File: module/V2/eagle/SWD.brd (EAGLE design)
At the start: 269.1 x 284.5 mm, 273 parts, among them J2 KLDX-0202-A, SW1 MF-SW-TACT-6MM, SW2 MF-SW-TACT-6MM, U1 P8X32A-Q44, U10 SN74LV4066APWR, U11 SN74LV4066APWR, U12 SN74LV4066APWR, U13 SN74LV4066APWR, U14 SN74LV4066APWR, U15 SN74LV4066APWR, U16 SN74LV4066APWR, U17 SN74LV4066APWR, U18 SN74LV4066APWR, U19 SN74LV4066APWR, U2 CAT24C512WI-GT3, U20 SN74LV4066APWR, U21 SN74LV4066APWR, U22 SN74LV4066APWR, U23 SN74LV4066APWR, U24 SSM6J507NU,LF, U25 SSM6J507NU,LF, U26 SSM6J507NU,LF, U27 SSM6J507NU,LF, U3 FT230XQ-R, U4 SN74LV4066APWR, U5 SN74LV4066APWR, U6 SN74LV4066APWR, U7 SN74LV4066APWR, U8 SN74LV4066APWR, U9 SN74LV4066APWR, X1 ABMM-6.000MHZ-B2-T

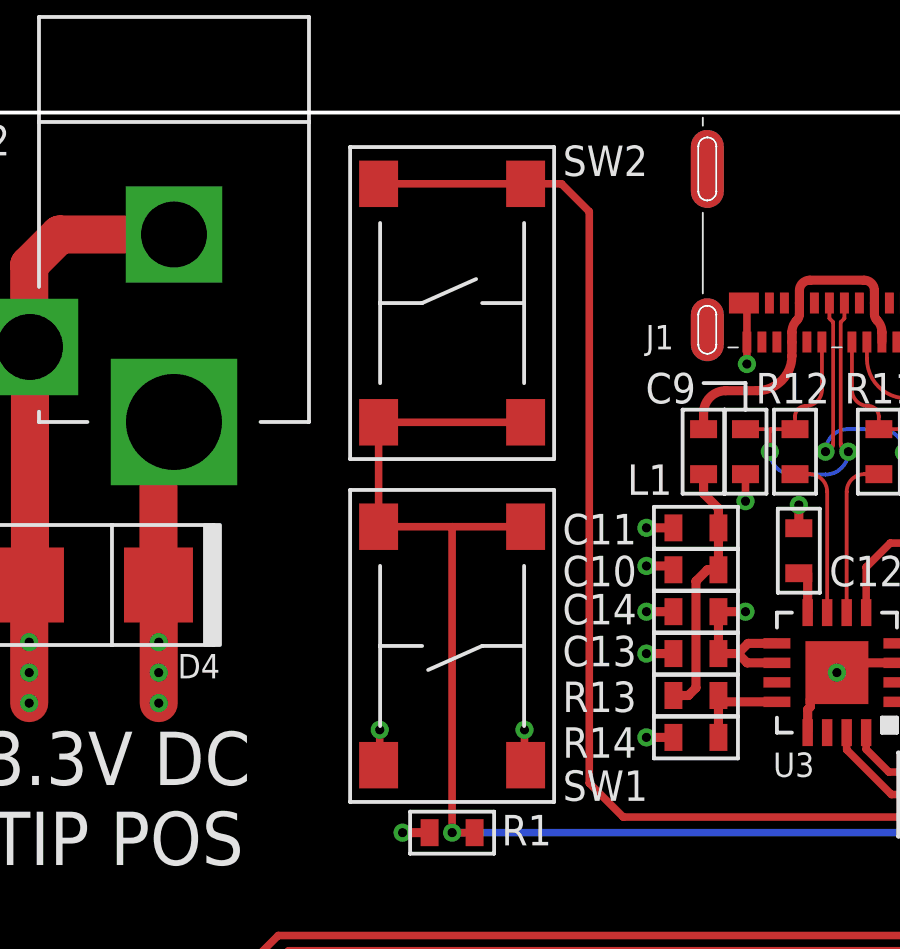
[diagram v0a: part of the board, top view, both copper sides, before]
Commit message: Fixed wire errors
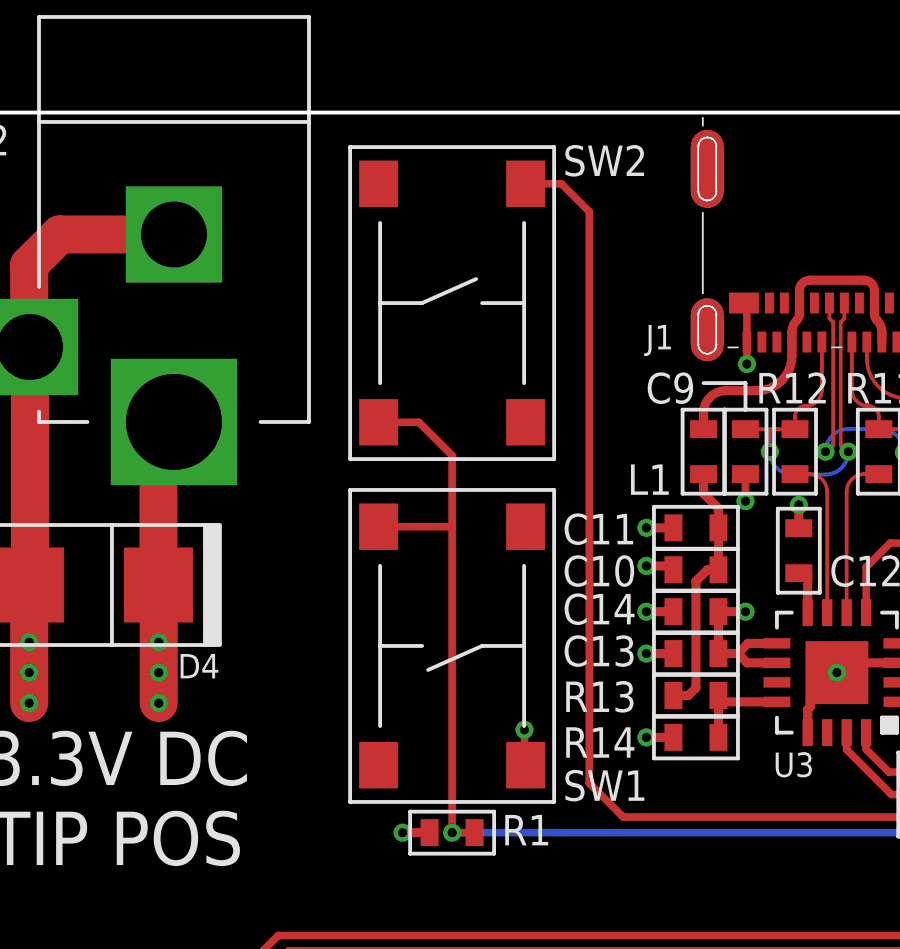
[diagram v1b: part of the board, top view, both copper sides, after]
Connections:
- net GND: no longer SW1.P$1
- net N$18: no longer SW2.P$3
- net RES: no longer SW1.P$4, SW2.P$2
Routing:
- net RES: track 86.6 -> 81.1 mm
- net N$18: track 37.9 -> 33.0 mm
- net GND: track 272.0 -> 270.8 mm, vias 68 -> 67
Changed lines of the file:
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@@
 <contactref element="SW1" pad="P$2"/>
 <contactref element="R1" pad="P$2"/>
-<contactref element="SW2" pad="P$2"/>
-<contactref element="SW2" pad="P$4"/>
-<wire x1="23.712" y1="274.155" x2="28.612" y2="274.155" width="0.254" layer="1"/>
-<wire x1="23.712" y1="274.155" x2="23.712" y2="270.675" width="0.254" layer="1"/>
-<contactref element="SW1" pad="P$4"/>
-<wire x1="28.612" y1="270.675" x2="26.162" y2="270.675" width="0.254" layer="1"/>
 <wire x1="26.162" y1="270.675" x2="23.712" y2="270.675" width="0.254" layer="1"/>
 <wire x1="26.912" y1="260.477" x2="26.162" y2="260.477" width="0.254" layer="1"/>
@@
 <wire x1="86.741" y1="260.477" x2="26.162" y2="260.477" width="0.254" layer="16"/>
 <via x="26.162" y="260.477" extent="1-16" drill="0.3048"/>
+<wire x1="26.162" y1="270.675" x2="26.162" y2="273.05" width="0.254" layer="1"/>
+<contactref element="SW2" pad="P$4"/>
+<wire x1="26.162" y1="273.05" x2="25.057" y2="274.155" width="0.254" layer="1"/>
+<wire x1="25.057" y1="274.155" x2="23.712" y2="274.155" width="0.254" layer="1"/>
 </signal>
 <signal name="3.3V">
@@
 <wire x1="45.974" y1="277.38" x2="45.974" y2="276.479" width="0.254" layer="1"/>
 <via x="45.974" y="276.479" extent="1-16" drill="0.3048"/>
-<contactref element="SW1" pad="P$1"/>
-<wire x1="23.712" y1="262.725" x2="23.749" y2="262.762" width="0.254" layer="1"/>
-<wire x1="23.749" y1="262.762" x2="23.749" y2="263.906" width="0.254" layer="1"/>
-<via x="23.749" y="263.906" extent="1-16" drill="0.3048"/>
 <wire x1="28.612" y1="262.725" x2="28.575" y2="262.762" width="0.254" layer="1"/>
 <wire x1="28.575" y1="262.762" x2="28.575" y2="263.906" width="0.254" layer="1"/>
@@
 <signal name="N$18">
 <contactref element="C15" pad="P$2"/>
-<contactref element="SW2" pad="P$1"/>
-<contactref element="SW2" pad="P$3"/>
 <wire x1="41.7322" y1="260.997" x2="31.865" y2="260.997" width="0.254" layer="1"/>
 <wire x1="31.865" y1="260.997" x2="30.734" y2="262.128" width="0.254" layer="1"/>
 <wire x1="30.734" y1="262.128" x2="30.734" y2="281.178" width="0.254" layer="1"/>
 <wire x1="30.734" y1="281.178" x2="29.807" y2="282.105" width="0.254" layer="1"/>
+<contactref element="SW2" pad="P$1"/>
 <wire x1="29.807" y1="282.105" x2="28.612" y2="282.105" width="0.254" layer="1"/>
-<wire x1="28.612" y1="282.105" x2="23.712" y2="282.105" width="0.254" layer="1"/>
 </signal>
 </signals>
